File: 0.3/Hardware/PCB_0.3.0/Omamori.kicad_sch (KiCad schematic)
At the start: 37 parts, among them J1 Conn_01x04_Female, J2 Conn_01x05_Female, J3 Conn_01x06_Female, J4 Conn_01x03_Female, U1 BQ25570, U2 ATtiny1626, U3 TS-1233

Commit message: Temporarily finished pcb design.
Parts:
- removed J1: Conn_01x04_Female, Connector_PinHeader_1.27mm:PinHeader_1x04_P1.27mm_Horizontal, symbol Connector:Conn_01x04_Female
- removed J2: Conn_01x05_Female, Connector_PinHeader_2.54mm:PinHeader_1x05_P2.54mm_Vertical, symbol Connector:Conn_01x05_Female
- removed J3: Conn_01x06_Female, Connector_PinHeader_2.54mm:PinHeader_1x06_P2.54mm_Vertical, symbol Connector:Conn_01x06_Female
- removed R_LED1, R_LED3: 500, Resistor_SMD:R_0603_1608Metric_Pad0.98x0.95mm_HandSolder, symbol Device:R
- removed R_LED2: 500, Resistor_SMD:R_0603_1608Metric_Pad1.05x0.95mm_HandSolder, symbol Device:R
- added J2: Conn_01x07_Female, Connector_PinHeader_2.54mm:PinHeader_1x07_P2.54mm_Vertical, symbol Connector:Conn_01x07_Female
- renumbered J4 to J1
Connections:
- net GND: now also J1.1 (Pin_1), U3.1 (A), J2.1 (Pin_1); no longer J1.3 (Pin_3), U3.2 (B)
- net Reset: now also U3.2 (B); no longer U3.1 (A)
- net Rx: now also U2.14 (PB0), J2.3 (Pin_3); no longer U2.13 (PB1)
- net Tx: now also U2.13 (PB1), J2.4 (Pin_4); no longer U2.14 (PB0)
- net VCC_LED1: now also D1.2 (A)
- net VCC_LED2: now also D2.2 (A)
- net VCC_LED3: now also D3.2 (A)
- net Vcc_ATTiny: now also J1.3 (Pin_3), J2.2 (Pin_2); no longer J1.1 (Pin_1)
- net at U2.6 (PA5): now also J2.7 (Pin_7)
- net at U2.7 (PA6): now also J2.6 (Pin_6)
- net at U2.8 (PA7): now also J2.5 (Pin_5)
- no-connect marks 2 -> 10
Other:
- note added: "Data Pins"
- note removed: "Serial Pins"
- moved on the sheet: J1

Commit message: Updated pcb.
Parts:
- D1, D2, D3: footprint LED_SMD:LED_1210_3225Metric_Pad1.42x2.65mm_HandSolder -> LED_SMD:LED_0805_2012Metric
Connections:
- net Rx: now also U2.10 (PB4); no longer U2.14 (PB0)
- net Tx: now also U2.9 (PB5); no longer U2.13 (PB1)
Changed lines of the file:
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@@
   (junction (at 127 139.7) (diameter 0) (color 0 0 0 0)
   )
+  (no_connect (at 204.47 124.46))
   (no_connect (at 173.99 129.54))
   (no_connect (at 173.99 132.08))
   (no_connect (at 173.99 127))
-  (no_connect (at 204.47 137.16))
-  (no_connect (at 204.47 134.62))
   (no_connect (at 204.47 132.08))
   (no_connect (at 173.99 124.46))
   (no_connect (at 204.47 129.54))
+  (no_connect (at 204.47 127))
   (no_connect (at 248.92 101.6))
   (no_connect (at 259.08 99.06))
+  (wire (pts (xy 223.52 91.44) (xy 223.52 134.62))
+    (stroke (width 0) (type default) (color 0 0 0 0))
+  )
   (wire (pts (xy 204.47 119.38) (xy 215.9 119.38))
     (stroke (width 0) (type default) (color 0 0 0 0))
@@
     (stroke (width 0) (type default) (color 0 0 0 0))
   )
-  (wire (pts (xy 223.52 91.44) (xy 223.52 124.46))
+  (wire (pts (xy 223.52 134.62) (xy 204.47 134.62))
     (stroke (width 0) (type default) (color 0 0 0 0))
   )
@@
     (stroke (width 0) (type default) (color 0 0 0 0))
   )
-  (wire (pts (xy 204.47 124.46) (xy 223.52 124.46))
-    (stroke (width 0) (type default) (color 0 0 0 0))
-  )
   (wire (pts (xy 210.82 91.44) (xy 223.52 91.44))
     (stroke (width 0) (type default) (color 0 0 0 0))
@@
     (stroke (width 0) (type default) (color 0 0 0 0))
   )
-  (wire (pts (xy 260.35 99.06) (xy 260.35 101.6))
-    (stroke (width 0) (type default) (color 0 0 0 0))
-  )
   (wire (pts (xy 127 106.68) (xy 118.11 106.68))
     (stroke (width 0) (type default) (color 0 0 0 0))
@@
     (stroke (width 0) (type default) (color 0 0 0 0))
   )
-  (wire (pts (xy 204.47 127) (xy 224.79 127))
-    (stroke (width 0) (type default) (color 0 0 0 0))
-  )
-  (wire (pts (xy 224.79 90.17) (xy 224.79 127))
+  (wire (pts (xy 224.79 90.17) (xy 224.79 137.16))
     (stroke (width 0) (type default) (color 0 0 0 0))
   )
@@
     (stroke (width 0) (type default) (color 0 0 0 0))
   )
-  (wire (pts (xy 262.89 99.06) (xy 260.35 99.06))
+  (wire (pts (xy 224.79 137.16) (xy 204.47 137.16))
     (stroke (width 0) (type default) (color 0 0 0 0))
   )
@@
     )
     (pin "1")
+    (pin "2")
     (pin "3")
     (pin "4")
-    (pin "2")
   )
   (symbol (lib_id "power:GND") (at 127 80.01 0) (unit 1)
@@
     (property "Reference" "D2" (id 0) (at 247.8786 132.08 0))
     (property "Value" "LED" (id 1) (at 250.19 132.08 0))
-    (property "Footprint" "LED_SMD:LED_1210_3225Metric_Pad1.42x2.65mm_HandSolder" (id 2) (at 248.92 124.46 0)
+    (property "Footprint" "LED_SMD:LED_0805_2012Metric" (id 2) (at 248.92 124.46 0)
       (effects (font (size 1.27 1.27)) hide)
     )
@@
     (property "Reference" "D1" (id 0) (at 255.4986 132.08 0))
     (property "Value" "LED" (id 1) (at 257.81 132.08 0))
-    (property "Footprint" "LED_SMD:LED_1210_3225Metric_Pad1.42x2.65mm_HandSolder" (id 2) (at 256.54 124.46 0)
+    (property "Footprint" "LED_SMD:LED_0805_2012Metric" (id 2) (at 256.54 124.46 0)
       (effects (font (size 1.27 1.27)) hide)
     )
@@
     (property "Reference" "D3" (id 0) (at 240.2586 132.08 0))
     (property "Value" "LED" (id 1) (at 242.57 132.08 0))
-    (property "Footprint" "LED_SMD:LED_1210_3225Metric_Pad1.42x2.65mm_HandSolder" (id 2) (at 241.3 124.46 0)
+    (property "Footprint" "LED_SMD:LED_0805_2012Metric" (id 2) (at 241.3 124.46 0)
       (effects (font (size 1.27 1.27)) hide)
     )
@@
     (pin "2")
   )
-  (symbol (lib_id "power:GND") (at 262.89 99.06 0) (unit 1)
+  (symbol (lib_id "power:GND") (at 260.35 101.6 0) (unit 1)
     (in_bom yes) (on_board yes) (fields_autoplaced)
-    (property "Reference" "#PWR0105" (id 0) (at 262.89 105.41 0)
-      (effects (font (size 1.27 1.27)) hide)
-    )
-    (property "Value" "GND" (id 1) (at 262.89 104.14 0))
-    (property "Footprint" "" (id 2) (at 262.89 99.06 0)
-      (effects (font (size 1.27 1.27)) hide)
-    )
-    (property "Datasheet" "" (id 3) (at 262.89 99.06 0)
+    (property "Reference" "#PWR0105" (id 0) (at 260.35 107.95 0)
+      (effects (font (size 1.27 1.27)) hide)
+    )
+    (property "Value" "GND" (id 1) (at 260.35 106.68 0))
+    (property "Footprint" "" (id 2) (at 260.35 101.6 0)
+      (effects (font (size 1.27 1.27)) hide)
+    )
+    (property "Datasheet" "" (id 3) (at 260.35 101.6 0)
       (effects (font (size 1.27 1.27)) hide)
     )
@@
     )
     (path "/00000000-0000-0000-0000-000062b5b151"
-      (reference "D1") (unit 1) (value "LED") (footprint "LED_SMD:LED_1210_3225Metric_Pad1.42x2.65mm_HandSolder")
+      (reference "D1") (unit 1) (value "LED") (footprint "LED_SMD:LED_0805_2012Metric")
     )
     (path "/00000000-0000-0000-0000-000062b45377"
-      (reference "D2") (unit 1) (value "LED") (footprint "LED_SMD:LED_1210_3225Metric_Pad1.42x2.65mm_HandSolder")
+      (reference "D2") (unit 1) (value "LED") (footprint "LED_SMD:LED_0805_2012Metric")
     )
     (path "/00000000-0000-0000-0000-000062d85c5c"
-      (reference "D3") (unit 1) (value "LED") (footprint "LED_SMD:LED_1210_3225Metric_Pad1.42x2.65mm_HandSolder")
+      (reference "D3") (unit 1) (value "LED") (footprint "LED_SMD:LED_0805_2012Metric")
     )
     (path "/dddf40b0-7751-48c9-b87e-63d26cb1192d"

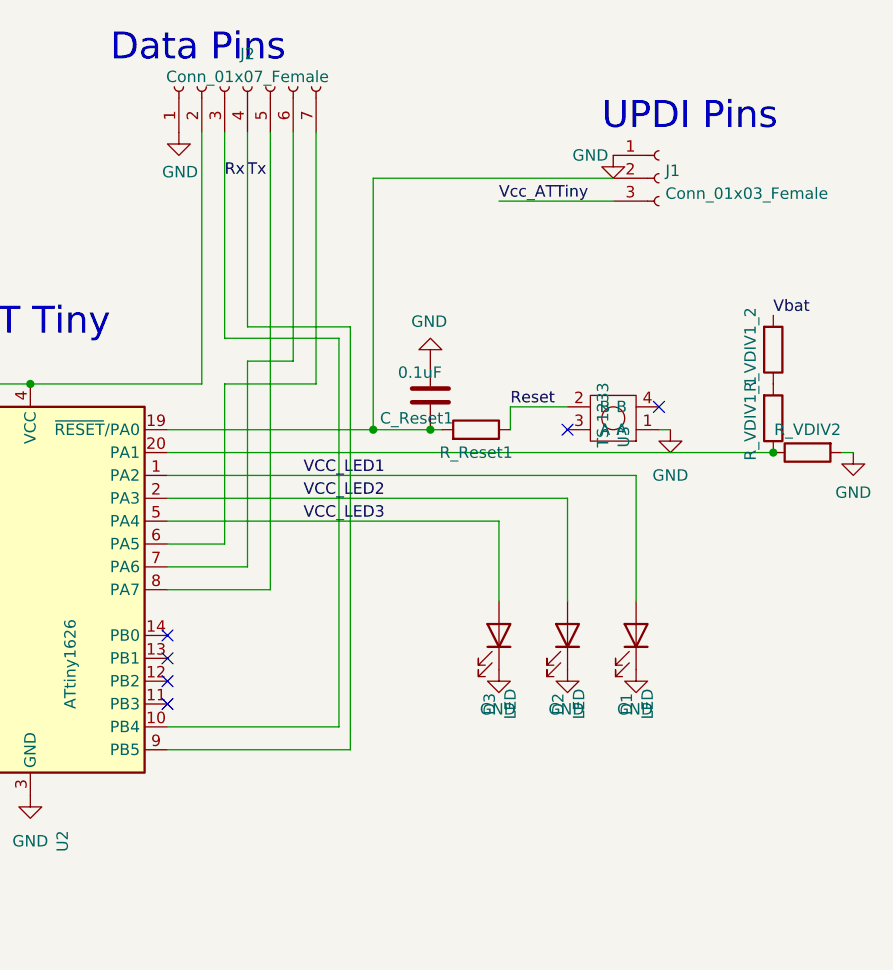
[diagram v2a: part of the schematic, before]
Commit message: Correct pcb design update for v3.
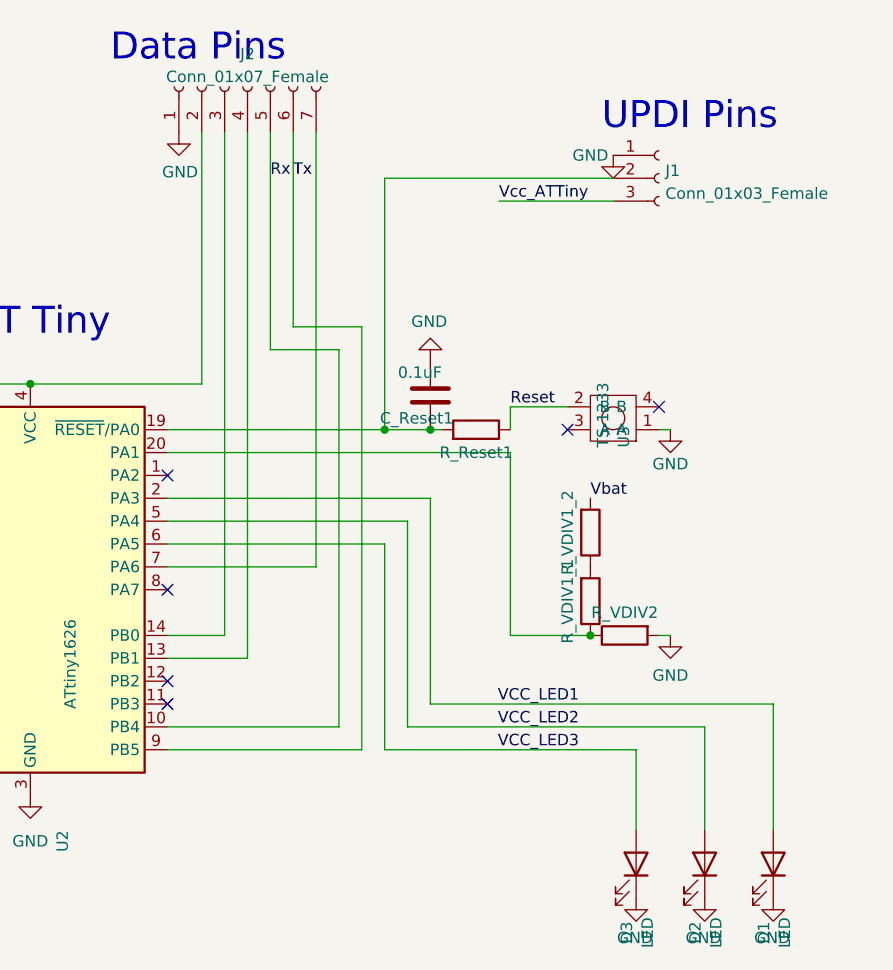
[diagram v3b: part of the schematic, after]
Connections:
- net Rx: now also J2.5 (Pin_5); no longer J2.3 (Pin_3)
- net Tx: now also J2.6 (Pin_6); no longer J2.4 (Pin_4)
- net VCC_LED1: now also U2.2 (PA3); no longer U2.1 (PA2)
- net VCC_LED2: now also U2.5 (PA4); no longer U2.2 (PA3)
- net VCC_LED3: now also U2.6 (PA5); no longer U2.5 (PA4)
- net at U2.8 (PA7): no longer J2.5 (Pin_5)
- net at U2.7 (PA6): now also J2.7 (Pin_7); no longer J2.6 (Pin_6)
- net at U2.13 (PB1): now also J2.4 (Pin_4)
- net at U2.14 (PB0): now also J2.3 (Pin_3)
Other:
- moved on the sheet: D1, D2, D3, R_VDIV1_1, R_VDIV1_2, R_VDIV2

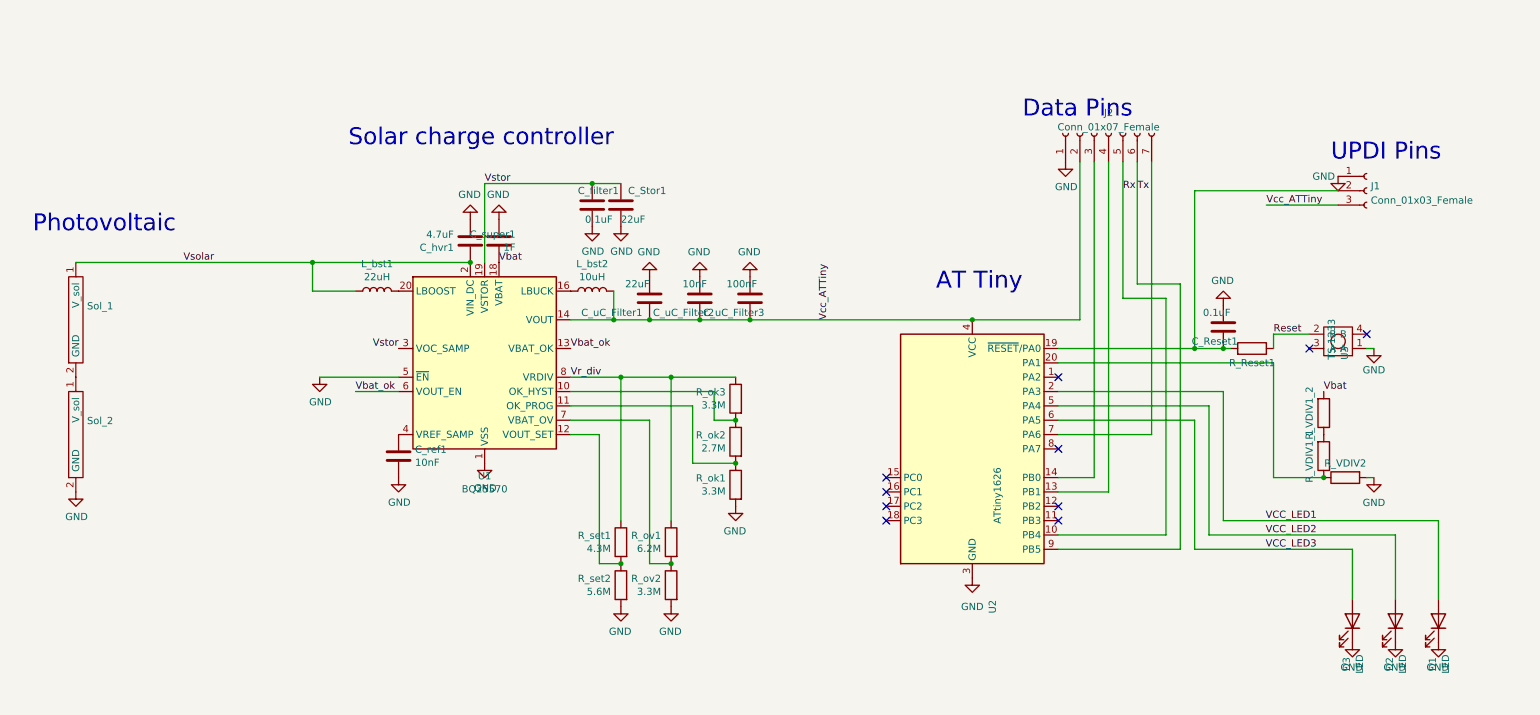
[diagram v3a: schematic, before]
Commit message: Updated to version, which got ordered on jlcpcb.
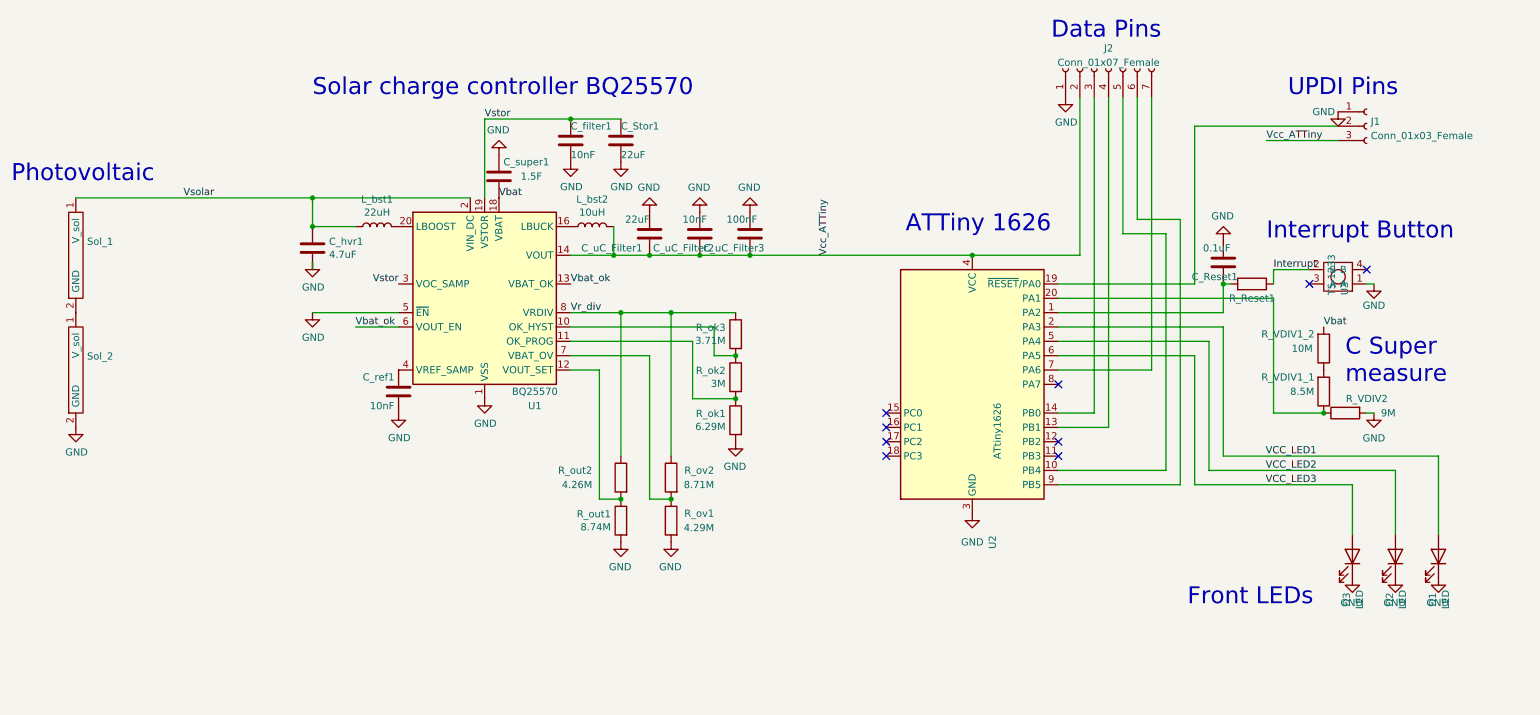
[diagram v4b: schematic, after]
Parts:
- C_filter1: value 0.1uF -> 10nF
- C_super1: value 1F -> 1.5F
- R_ok1: value 3.3M -> 6.29M
- R_ok2: value 2.7M -> 3M
- R_ok3: value 3.3M -> 3.71M
- R_out1: renamed from R_set2; value 5.6M -> 8.74M
- R_out2: renamed from R_set1; value 4.3M -> 4.26M
- R_ov1: renamed from R_ov2; value 3.3M -> 4.29M
- R_ov2: renamed from R_ov1; value 6.2M -> 8.71M
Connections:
- net at C_Reset1.1, R_Reset1.2: now also U2.1 (PA2); no longer J1.2 (Pin_2), U2.19 (~{RESET}/PA0)
- net Reset renamed Interrupt
- net Rx: no longer names the net of J2.5 (Pin_5), U2.10 (PB4)
- net Tx: no longer names the net of J2.6 (Pin_6), U2.9 (PB5)
- new net: J1.2 (Pin_2), U2.19 (~{RESET}/PA0)
- no-connect marks 10 -> 9
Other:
- note added: "ATTiny 1626"
- note added: "C Super measure"
- note added: "Front LEDs"
- note added: "Interrupt Button"
- note added: "Solar charge controller BQ25570"
- note removed: "AT Tiny"
- note removed: "Solar charge controller"
- moved on the sheet: C_Reset1, C_Stor1, C_filter1, C_hvr1, C_ref1, C_super1, C_uC_Filter1, C_uC_Filter2, C_uC_Filter3, D1, D2, D3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
